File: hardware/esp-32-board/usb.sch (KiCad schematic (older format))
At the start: 10 parts, among them J5 USB_B_Micro, Q1 BCR129S, U2 USBLC6-2SC6, U3 FT232RL

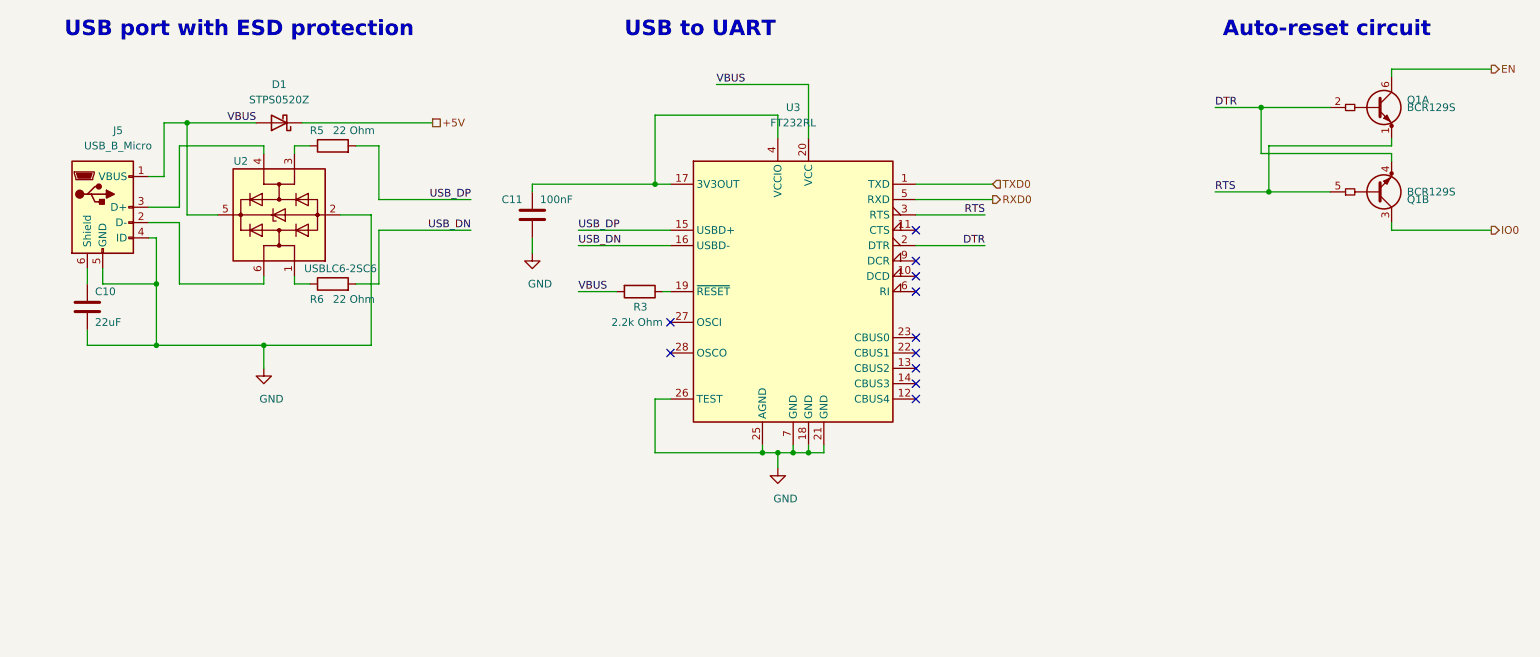
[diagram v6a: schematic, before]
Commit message: Replace power switch with jumper, add RX/TX leds
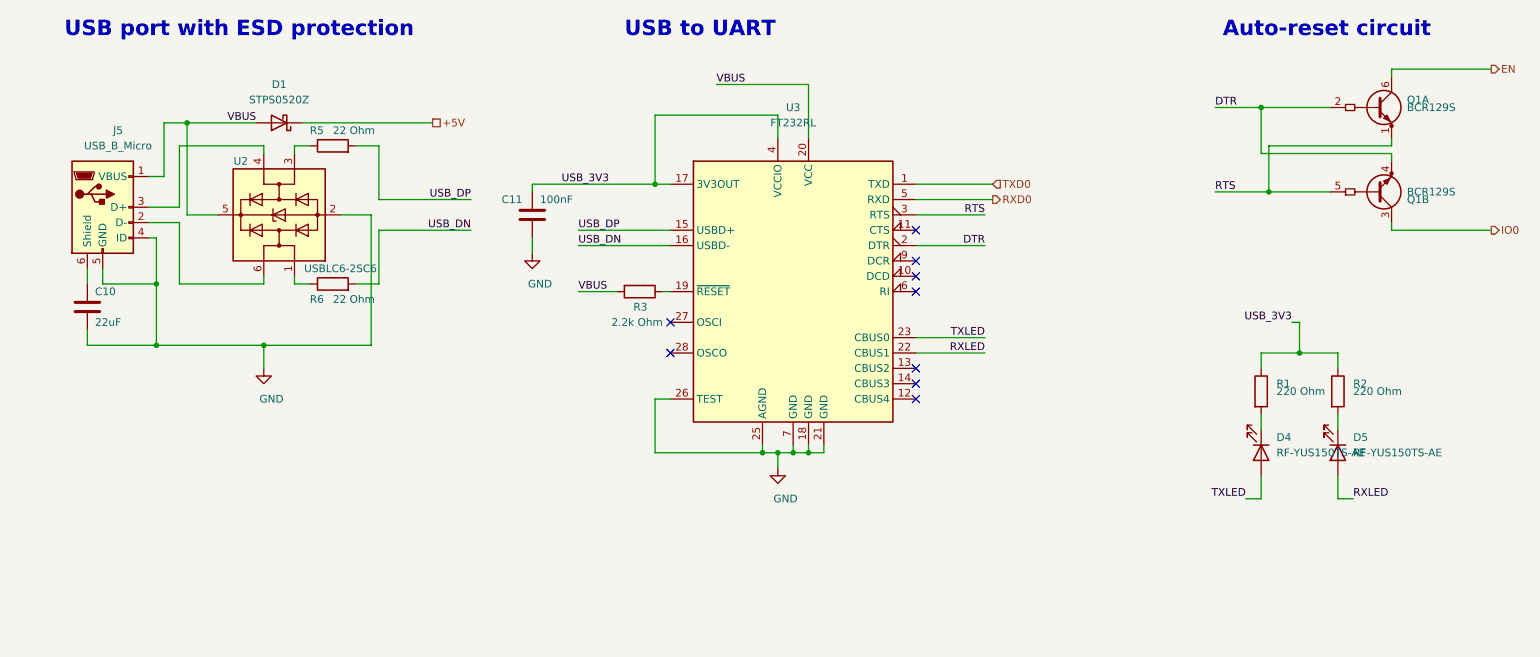
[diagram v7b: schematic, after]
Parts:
- added D4, D5: RF-YUS150TS-AE, LED_SMD:LED_1206_3216Metric_Pad1.42x1.75mm_HandSolder, symbol Device:LED
- added R1, R2: 220 Ohm, Resistor_SMD:R_0805_2012Metric_Pad1.20x1.40mm_HandSolder, symbol Device:R
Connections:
- net USB_3V3: now reaches C11.1, U3.17 (3V3OUT), U3.4 (VCCIO)
- net USB_3V3: now also R1.1, R2.1
- net RXLED: now reaches U3.22 (CBUS1)
- net RXLED: now also D5.2 (A)
- net TXLED: now reaches U3.23 (CBUS0)
- net TXLED: now also D4.2 (A)
- new net: D4.1 (K), R1.2
- new net: D5.1 (K), R2.2
- no-connect marks 11 -> 9
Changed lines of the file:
@@
 Wire Wire Line
 	9950 1850 10600 1850
-$Comp
-L power:GND #PWR?
-U 1 1 5FFC9960
-P 2600 3800
-AR Path="/5FFC9960" Ref="#PWR?"  Part="1"
-AR Path="/5FF73D59/5FFC9960" Ref="#PWR023"  Part="1"
-F 0 "#PWR023" H 2600 3550 50  0001 C CNN
-F 1 "GND" H 2650 3600 50  0000 C CNN
-F 2 "" H 2600 3800 50  0001 C CNN
-F 3 "" H 2600 3800 50  0001 C CNN
-	1    2600 3800
-	1    0    0    -1
-$EndComp
-Wire Wire Line
-	2600 3800 2600 3650
 Text Label 5550 1950 0    50   ~ 0
 VBUS
@@
 Wire Wire Line
 	1450 3150 1450 3250
-Wire Wire Line
-	1450 3550 1450 3650
 $Comp
 L Power_Protection:USBLC6-2SC6 U2
@@
 	3350 2900 3950 2900
 Wire Wire Line
-	3300 3650 2600 3650
-Connection ~ 1900 3650
-Wire Wire Line
 	3100 2800 3300 2800
 Wire Wire Line
 	1950 2200 2100 2200
-Wire Wire Line
-	3300 2800 3300 3650
 Wire Wire Line
 	2300 2800 2100 2800
@@
 Wire Wire Line
 	2100 2200 2550 2200
-Connection ~ 2600 3650
-Wire Wire Line
-	1900 3650 2600 3650
-Wire Wire Line
-	1450 3650 1900 3650
 Wire Wire Line
 	1550 3150 1550 3250
@@
 	1550 3250 1900 3250
 Connection ~ 1900 3250
-Wire Wire Line
-	1900 3250 1900 3650
 Wire Wire Line
 	2850 2200 3700 2200
@@
 NoConn ~ 6850 3200
 NoConn ~ 6850 3300
-NoConn ~ 6850 3600
-NoConn ~ 6850 3700
 NoConn ~ 6850 3800
 NoConn ~ 6850 3900
@@
 NoConn ~ 5250 3500
 NoConn ~ 5250 3700
+Text Label 7300 3700 2    50   ~ 0
+RXLED
+Text Label 7300 3600 2    50   ~ 0
+TXLED
+Wire Wire Line
+	6850 3600 7300 3600
+Wire Wire Line
+	7300 3700 6850 3700
+$Comp
+L Device:LED D4
+U 1 1 5FFCB60F
+P 9100 4350
+F 0 "D4" V 9000 4450 50  0000 L CNN
+F 1 "RF-YUS150TS-AE" V 9100 4450 50  0000 L CNN
+F 2 "LED_SMD:LED_1206_3216Metric_Pad1.42x1.75mm_HandSolder" H 9100 4350 50  0001 C CNN
+F 3 "https://www.tme.eu/Document/4237cf95222820e492ff101ceed40a8c/RF-YUS150TS-AE.pdf" H 9100 4350 50  0001 C CNN
+F 4 "tme.eu" H 9100 4350 50  0001 C CNN "Vendor"
+F 5 "https://www.tme.eu/pl/details/rf-yus150ts-ae/diody-led-smd-kolorowe/refond/" H 9100 4350 50  0001 C CNN "VendorLink"
+	1    9100 4350
+	0    1    1    0
+$EndComp
+$Comp
+L Device:LED D5
+U 1 1 5FFCC087
+P 9600 4350
+F 0 "D5" V 9500 4450 50  0000 L CNN
+F 1 "RF-YUS150TS-AE" V 9600 4450 50  0000 L CNN
+F 2 "LED_SMD:LED_1206_3216Metric_Pad1.42x1.75mm_HandSolder" H 9600 4350 50  0001 C CNN
+F 3 "https://www.tme.eu/Document/4237cf95222820e492ff101ceed40a8c/RF-YUS150TS-AE.pdf" H 9600 4350 50  0001 C CNN
+F 4 "tme.eu" H 9600 4350 50  0001 C CNN "Vendor"
+F 5 "https://www.tme.eu/pl/details/rf-yus150ts-ae/diody-led-smd-kolorowe/refond/" H 9600 4350 50  0001 C CNN "VendorLink"
+	1    9600 4350
+	0    1    1    0
+$EndComp
+Text Label 9000 4650 2    50   ~ 0
+TXLED
+Wire Wire Line
+	9000 4650 9100 4650
+Wire Wire Line
+	9100 4650 9100 4500
+Text Label 9700 4650 0    50   ~ 0
+RXLED
+Wire Wire Line
+	9600 4500 9600 4650
+Wire Wire Line
+	9600 4650 9700 4650
+Wire Wire Line
+	9100 3800 9100 3700
+Wire Wire Line
+	9100 3700 9350 3700
+Wire Wire Line
+	9600 3700 9600 3800
+Wire Wire Line
+	9350 3700 9350 3500
+Connection ~ 9350 3700
+Wire Wire Line
+	9350 3700 9600 3700
+$Comp
+L Device:R R1
+U 1 1 5FFD83B8
+P 9100 3950
+F 0 "R1" H 9200 4000 50  0000 L CNN
+F 1 "220 Ohm" H 9200 3950 50  0000 L CNN
+F 2 "Resistor_SMD:R_0805_2012Metric_Pad1.20x1.40mm_HandSolder" V 9030 3950 50  0001 C CNN
+F 3 "~" H 9100 3950 50  0001 C CNN
+F 4 "avt.pl" H 9100 3950 50  0001 C CNN "Vendor"
+F 5 "https://sklep.avt.pl/avt701-805.html" H 9100 3950 50  0001 C CNN "VendorLink"
+	1    9100 3950
+	1    0    0    -1
+$EndComp
+$Comp
+L Device:R R2
+U 1 1 5FFDD2E6
+P 9600 3950
+F 0 "R2" H 9700 4000 50  0000 L CNN
+F 1 "220 Ohm" H 9700 3950 50  0000 L CNN
+F 2 "Resistor_SMD:R_0805_2012Metric_Pad1.20x1.40mm_HandSolder" V 9530 3950 50  0001 C CNN
+F 3 "~" H 9600 3950 50  0001 C CNN
+F 4 "avt.pl" H 9600 3950 50  0001 C CNN "Vendor"
+F 5 "https://sklep.avt.pl/avt701-805.html" H 9600 3950 50  0001 C CNN "VendorLink"
+	1    9600 3950
+	1    0    0    -1
+$EndComp
+Wire Wire Line
+	9100 4100 9100 4200
+Wire Wire Line
+	9600 4100 9600 4200
+Text Label 4850 2600 2    50   ~ 0
+USB_3V3
+Text Label 9300 3500 2    50   ~ 0
+USB_3V3
+Wire Wire Line
+	9350 3500 9300 3500
+Wire Wire Line
+	1900 3250 1900 3650
+Wire Wire Line
+	1450 3650 1900 3650
+Wire Wire Line
+	1900 3650 2600 3650
+Connection ~ 2600 3650
+Wire Wire Line
+	3300 2800 3300 3650
+Connection ~ 1900 3650
+Wire Wire Line
+	3300 3650 2600 3650
+Wire Wire Line
+	1450 3550 1450 3650
+Wire Wire Line
+	2600 3800 2600 3650
+$Comp
+L power:GND #PWR?
+U 1 1 5FFC9960
+P 2600 3800
+AR Path="/5FFC9960" Ref="#PWR?"  Part="1"
+AR Path="/5FF73D59/5FFC9960" Ref="#PWR023"  Part="1"
+F 0 "#PWR023" H 2600 3550 50  0001 C CNN
+F 1 "GND" H 2650 3600 50  0000 C CNN
+F 2 "" H 2600 3800 50  0001 C CNN
+F 3 "" H 2600 3800 50  0001 C CNN
+	1    2600 3800
+	1    0    0    -1
+$EndComp
 $EndSCHEMATC

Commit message: Move LEDs
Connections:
- net RXLED: now also R2.2; no longer D5.2 (A)
- net TXLED: now also R1.2; no longer D4.2 (A)
- net USB_3V3: now also D4.1 (K), D5.1 (K); no longer R1.1, R2.1
- new net: D4.2 (A), R1.1
- new net: D5.2 (A), R2.1
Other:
- moved on the sheet: D4, D5, R1, R2
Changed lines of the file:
@@
 L Device:LED D4
 U 1 1 5FFCB60F
-P 9100 4350
-F 0 "D4" V 9000 4450 50  0000 L CNN
-F 1 "RF-YUS150TS-AE" V 9100 4450 50  0000 L CNN
-F 2 "LED_SMD:LED_1206_3216Metric_Pad1.42x1.75mm_HandSolder" H 9100 4350 50  0001 C CNN
-F 3 "https://www.tme.eu/Document/4237cf95222820e492ff101ceed40a8c/RF-YUS150TS-AE.pdf" H 9100 4350 50  0001 C CNN
-F 4 "tme.eu" H 9100 4350 50  0001 C CNN "Vendor"
-F 5 "https://www.tme.eu/pl/details/rf-yus150ts-ae/diody-led-smd-kolorowe/refond/" H 9100 4350 50  0001 C CNN "VendorLink"
-	1    9100 4350
+P 9100 3950
+F 0 "D4" V 9000 4050 50  0000 L CNN
+F 1 "RF-YUS150TS-AE" V 9100 4050 50  0000 L CNN
+F 2 "LED_SMD:LED_1206_3216Metric_Pad1.42x1.75mm_HandSolder" H 9100 3950 50  0001 C CNN
+F 3 "https://www.tme.eu/Document/4237cf95222820e492ff101ceed40a8c/RF-YUS150TS-AE.pdf" H 9100 3950 50  0001 C CNN
+F 4 "tme.eu" H 9100 3950 50  0001 C CNN "Vendor"
+F 5 "https://www.tme.eu/pl/details/rf-yus150ts-ae/diody-led-smd-kolorowe/refond/" H 9100 3950 50  0001 C CNN "VendorLink"
+	1    9100 3950
 	0    1    1    0
 $EndComp
@@
 L Device:LED D5
 U 1 1 5FFCC087
-P 9600 4350
-F 0 "D5" V 9500 4450 50  0000 L CNN
-F 1 "RF-YUS150TS-AE" V 9600 4450 50  0000 L CNN
-F 2 "LED_SMD:LED_1206_3216Metric_Pad1.42x1.75mm_HandSolder" H 9600 4350 50  0001 C CNN
-F 3 "https://www.tme.eu/Document/4237cf95222820e492ff101ceed40a8c/RF-YUS150TS-AE.pdf" H 9600 4350 50  0001 C CNN
-F 4 "tme.eu" H 9600 4350 50  0001 C CNN "Vendor"
-F 5 "https://www.tme.eu/pl/details/rf-yus150ts-ae/diody-led-smd-kolorowe/refond/" H 9600 4350 50  0001 C CNN "VendorLink"
-	1    9600 4350
+P 9600 3950
+F 0 "D5" V 9500 4050 50  0000 L CNN
+F 1 "RF-YUS150TS-AE" V 9600 4050 50  0000 L CNN
+F 2 "LED_SMD:LED_1206_3216Metric_Pad1.42x1.75mm_HandSolder" H 9600 3950 50  0001 C CNN
+F 3 "https://www.tme.eu/Document/4237cf95222820e492ff101ceed40a8c/RF-YUS150TS-AE.pdf" H 9600 3950 50  0001 C CNN
+F 4 "tme.eu" H 9600 3950 50  0001 C CNN "Vendor"
+F 5 "https://www.tme.eu/pl/details/rf-yus150ts-ae/diody-led-smd-kolorowe/refond/" H 9600 3950 50  0001 C CNN "VendorLink"
+	1    9600 3950
 	0    1    1    0
 $EndComp
@@
 L Device:R R1
 U 1 1 5FFD83B8
-P 9100 3950
-F 0 "R1" H 9200 4000 50  0000 L CNN
-F 1 "220 Ohm" H 9200 3950 50  0000 L CNN
-F 2 "Resistor_SMD:R_0805_2012Metric_Pad1.20x1.40mm_HandSolder" V 9030 3950 50  0001 C CNN
-F 3 "~" H 9100 3950 50  0001 C CNN
-F 4 "avt.pl" H 9100 3950 50  0001 C CNN "Vendor"
-F 5 "https://sklep.avt.pl/avt701-805.html" H 9100 3950 50  0001 C CNN "VendorLink"
-	1    9100 3950
+P 9100 4350
+F 0 "R1" H 9200 4400 50  0000 L CNN
+F 1 "220 Ohm" H 9200 4350 50  0000 L CNN
+F 2 "Resistor_SMD:R_0805_2012Metric_Pad1.20x1.40mm_HandSolder" V 9030 4350 50  0001 C CNN
+F 3 "~" H 9100 4350 50  0001 C CNN
+F 4 "avt.pl" H 9100 4350 50  0001 C CNN "Vendor"
+F 5 "https://sklep.avt.pl/avt701-805.html" H 9100 4350 50  0001 C CNN "VendorLink"
+	1    9100 4350
 	1    0    0    -1
 $EndComp
@@
 L Device:R R2
 U 1 1 5FFDD2E6
-P 9600 3950
-F 0 "R2" H 9700 4000 50  0000 L CNN
-F 1 "220 Ohm" H 9700 3950 50  0000 L CNN
-F 2 "Resistor_SMD:R_0805_2012Metric_Pad1.20x1.40mm_HandSolder" V 9530 3950 50  0001 C CNN
-F 3 "~" H 9600 3950 50  0001 C CNN
-F 4 "avt.pl" H 9600 3950 50  0001 C CNN "Vendor"
-F 5 "https://sklep.avt.pl/avt701-805.html" H 9600 3950 50  0001 C CNN "VendorLink"
-	1    9600 3950
+P 9600 4350
+F 0 "R2" H 9700 4400 50  0000 L CNN
+F 1 "220 Ohm" H 9700 4350 50  0000 L CNN
+F 2 "Resistor_SMD:R_0805_2012Metric_Pad1.20x1.40mm_HandSolder" V 9530 4350 50  0001 C CNN
+F 3 "~" H 9600 4350 50  0001 C CNN
+F 4 "avt.pl" H 9600 4350 50  0001 C CNN "Vendor"
+F 5 "https://sklep.avt.pl/avt701-805.html" H 9600 4350 50  0001 C CNN "VendorLink"
+	1    9600 4350
 	1    0    0    -1
 $EndComp
